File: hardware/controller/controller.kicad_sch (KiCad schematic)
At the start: 94 parts, among them J1 Bus_PCI_Express_x1, J2 USB, J4 BM03B-SRSS-TB(LF)(SN), J6 RJ45_Hanrun_HR913550A_Horizon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, Q1 2N7002, Q2 2N7002, SW1 434133025816, SW2 434133025816, SW3 SW_Push, U1 RP2350A, U2 AP7361C-33E, U3 W25Q128JVSIQ, U4 W6100-L, U5 RPi Radio Module 2, X1 12MHz, Y2 X322525MRB4SI

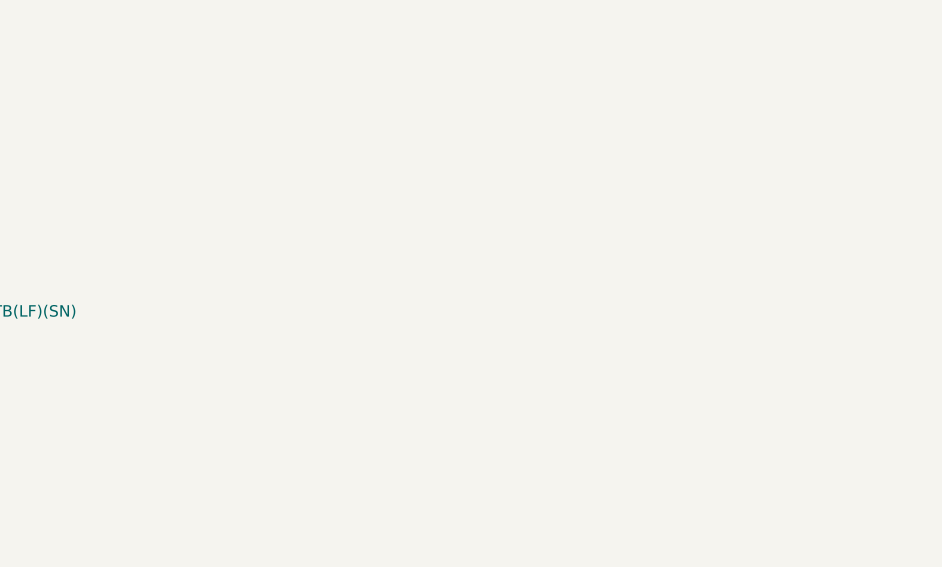
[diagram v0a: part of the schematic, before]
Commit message: feat(controller): add UART for UPS
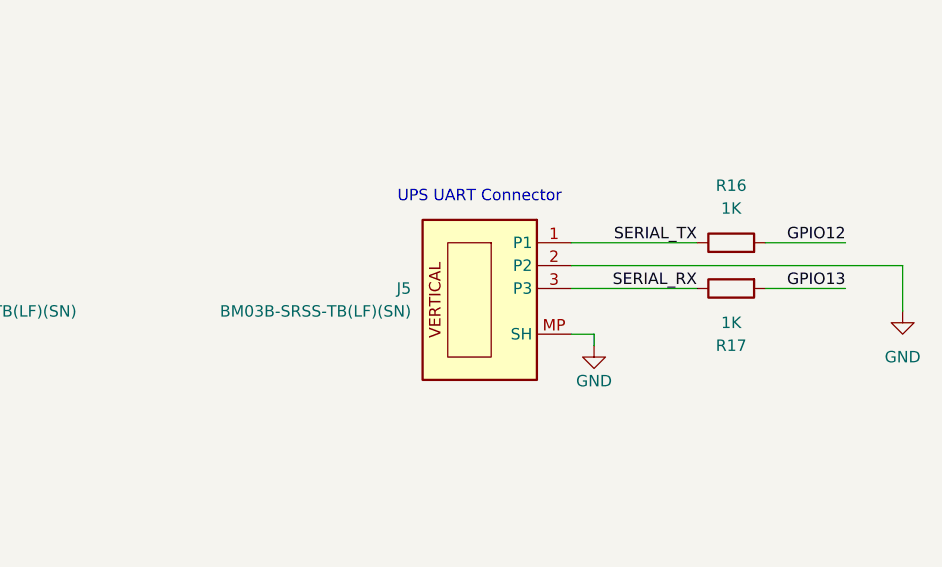
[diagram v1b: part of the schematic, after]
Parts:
- added J5: BM03B-SRSS-TB(LF)(SN), Connector_JST:JST_SH_BM03B-SRSS-TB_1x03-1MP_P1.00mm_Vertical, symbol RPI_DB:Connectors | Rectangular/RP-01EKJ1-8V9SV1
- added R16, R17: 1K, Local Library:R_0402_1005Metric, symbol Device:R
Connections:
- net GND: now also J5.2 (P2), J5.MP (SH)
- net GPIO12: now also R16.2
- net GPIO13: now also R17.2
- new net SERIAL_RX: J5.3 (P3), R17.1
- new net SERIAL_TX: J5.1 (P1), R16.1
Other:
- note added: "UPS UART Connector"
